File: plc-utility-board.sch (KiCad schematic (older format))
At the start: 11 parts, among them J1 Screw_Terminal_01x02, J10 Screw_Terminal_01x03, J11 Screw_Terminal_01x02, J2 Screw_Terminal_01x08, J3 Screw_Terminal_01x04, J4 Screw_Terminal_01x08, J5 Screw_Terminal_01x04, J6 Conn_01x03_Male, J7 Conn_01x03_Male, J8 Screw_Terminal_01x03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

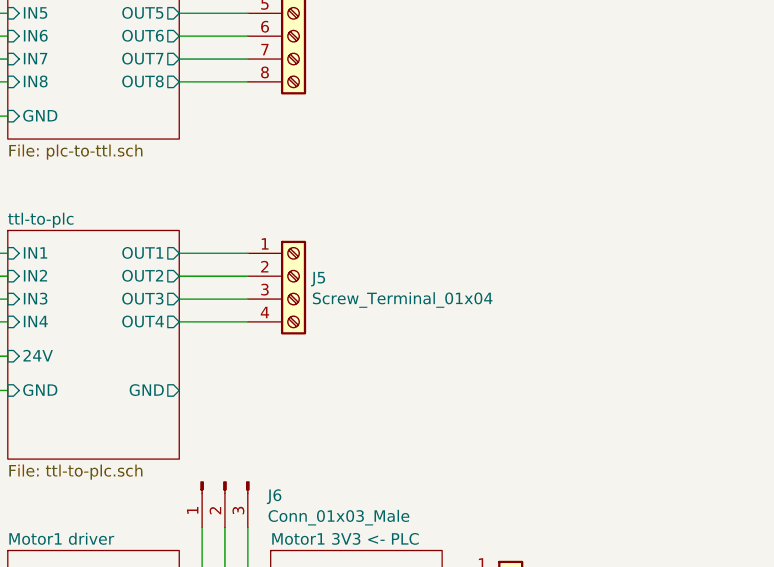
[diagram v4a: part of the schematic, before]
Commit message: Added switch for selecting Low/High power motor. Added thermal pads around motor controllers.
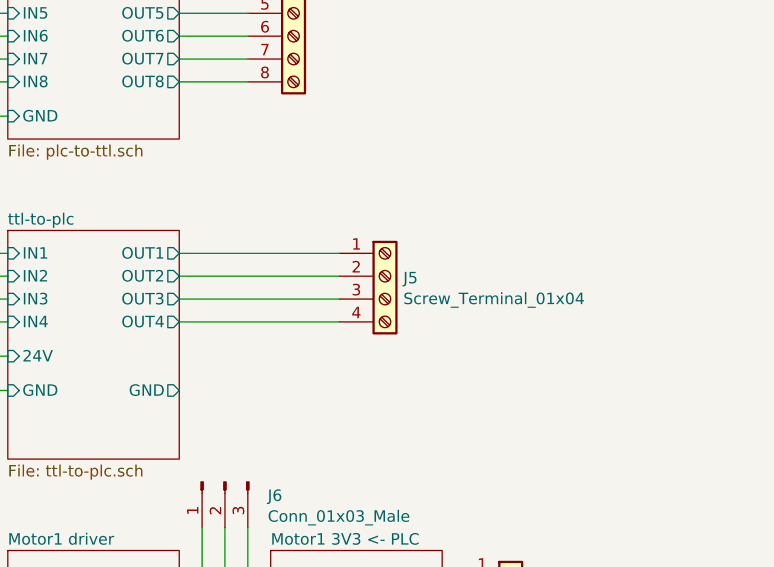
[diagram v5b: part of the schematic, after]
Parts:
- J5: footprint TerminalBlock_Phoenix:TerminalBlock_Phoenix_MKDS-1,5-4-5.08_1x04_P5.08mm_Horizontal -> (none)
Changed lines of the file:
@@
 	5050 3600 5050 3950
-Wire Wire Line
-	4850 2400 5150 2400
-Wire Wire Line
-	4850 2500 5150 2500
-Wire Wire Line
-	4850 2600 5150 2600
-Wire Wire Line
-	5150 2700 4850 2700
 Wire Wire Line
 	3050 2850 3050 3800
@@
 Wire Wire Line
 	2850 4100 2850 5700
+Wire Wire Line
+	4850 2400 5550 2400
+Wire Wire Line
+	4850 2500 5550 2500
 $Comp
 L mylib:Screw_Terminal_01x04 J5
-U 1 1 5BEF4585
-P 5350 2500
-F 0 "J5" H 5430 2492 50  0000 L CNN
-F 1 "Screw_Terminal_01x04" H 5430 2401 50  0000 L CNN
-F 2 "TerminalBlock_Phoenix:TerminalBlock_Phoenix_MKDS-1,5-4-5.08_1x04_P5.08mm_Horizontal" H 5350 2500 50  0001 C CNN
-F 3 "~" H 5350 2500 50  0001 C CNN
-	1    5350 2500
+U 1 1 5BF59862
+P 5750 2500
+F 0 "J5" H 5830 2492 50  0000 L CNN
+F 1 "Screw_Terminal_01x04" H 5830 2401 50  0000 L CNN
+F 2 "" H 5750 2500 50  0001 C CNN
+F 3 "~" H 5750 2500 50  0001 C CNN
+	1    5750 2500
 	1    0    0    -1
 $EndComp
+Wire Wire Line
+	4850 2700 5550 2700
+Wire Wire Line
+	4850 2600 5550 2600
 $EndSCHEMATC

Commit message: Added GND zones. Changed priority of motor controllers voltage zones to 1. Added labels to terminal blocks
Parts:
- J5: footprint (none) -> TerminalBlock_Phoenix:TerminalBlock_Phoenix_MKDS-1,5-4-5.08_1x04_P5.08mm_Horizontal
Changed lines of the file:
@@
 F 0 "J5" H 5830 2492 50  0000 L CNN
 F 1 "Screw_Terminal_01x04" H 5830 2401 50  0000 L CNN
-F 2 "" H 5750 2500 50  0001 C CNN
+F 2 "TerminalBlock_Phoenix:TerminalBlock_Phoenix_MKDS-1,5-4-5.08_1x04_P5.08mm_Horizontal" H 5750 2500 50  0001 C CNN
 F 3 "~" H 5750 2500 50  0001 C CNN
 	1    5750 2500

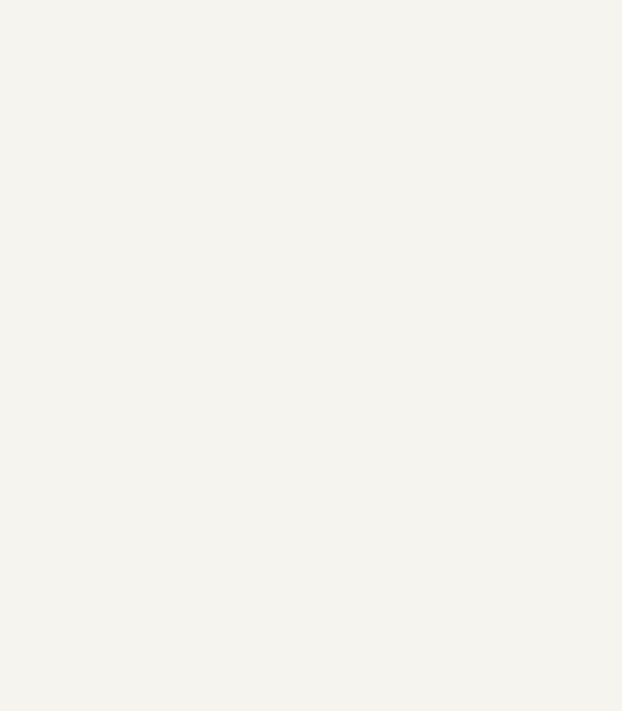
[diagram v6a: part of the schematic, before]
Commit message: Added mounting holes for M3 screws. Performed DRC check.
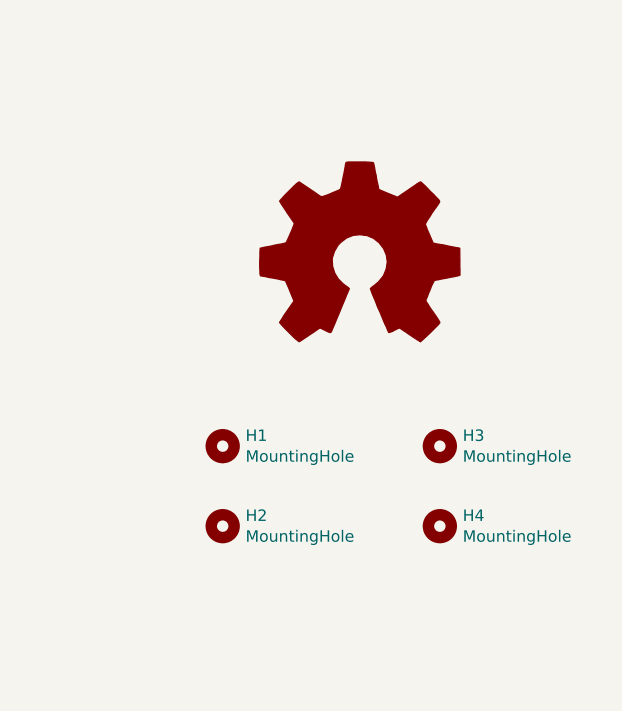
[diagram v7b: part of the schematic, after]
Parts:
- added H1, H2, H3, H4: MountingHole, MountingHole:MountingHole_3.2mm_M3_Pad_Via, symbol Mechanical:MountingHole
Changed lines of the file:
@@
 Wire Wire Line
 	4850 2600 5550 2600
+$Comp
+L Mechanical:MountingHole H1
+U 1 1 5BF5CA64
+P 8500 4350
+F 0 "H1" H 8600 4396 50  0000 L CNN
+F 1 "MountingHole" H 8600 4305 50  0000 L CNN
+F 2 "MountingHole:MountingHole_3.2mm_M3_Pad_Via" H 8500 4350 50  0001 C CNN
+F 3 "~" H 8500 4350 50  0001 C CNN
+	1    8500 4350
+	1    0    0    -1
+$EndComp
+$Comp
+L Mechanical:MountingHole H3
+U 1 1 5BF5CABE
+P 9450 4350
+F 0 "H3" H 9550 4396 50  0000 L CNN
+F 1 "MountingHole" H 9550 4305 50  0000 L CNN
+F 2 "MountingHole:MountingHole_3.2mm_M3_Pad_Via" H 9450 4350 50  0001 C CNN
+F 3 "~" H 9450 4350 50  0001 C CNN
+	1    9450 4350
+	1    0    0    -1
+$EndComp
+$Comp
+L Mechanical:MountingHole H2
+U 1 1 5BF5CB0C
+P 8500 4700
+F 0 "H2" H 8600 4746 50  0000 L CNN
+F 1 "MountingHole" H 8600 4655 50  0000 L CNN
+F 2 "MountingHole:MountingHole_3.2mm_M3_Pad_Via" H 8500 4700 50  0001 C CNN
+F 3 "~" H 8500 4700 50  0001 C CNN
+	1    8500 4700
+	1    0    0    -1
+$EndComp
+$Comp
+L Mechanical:MountingHole H4
+U 1 1 5BF5CB56
+P 9450 4700
+F 0 "H4" H 9550 4746 50  0000 L CNN
+F 1 "MountingHole" H 9550 4655 50  0000 L CNN
+F 2 "MountingHole:MountingHole_3.2mm_M3_Pad_Via" H 9450 4700 50  0001 C CNN
+F 3 "~" H 9450 4700 50  0001 C CNN
+	1    9450 4700
+	1    0    0    -1
+$EndComp
+$Comp
+L Graphic:Logo_Open_Hardware_Large #LOGO1
+U 1 1 5BF5D0FC
+P 9100 3550
+F 0 "#LOGO1" H 9100 4050 50  0001 C CNN
+F 1 "Logo_Open_Hardware_Large" H 9100 3150 50  0001 C CNN
+F 2 "plc-utility-board:logo" H 9100 3550 50  0001 C CNN
+F 3 "~" H 9100 3550 50  0001 C CNN
+	1    9100 3550
+	1    0    0    -1
+$EndComp
 $EndSCHEMATC
